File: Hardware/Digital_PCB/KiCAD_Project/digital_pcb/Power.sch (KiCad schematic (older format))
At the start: 24 parts, among them J6 Power, J7 Power Switch, U10 TPS793, U11 TPS1H000, U7 LT1521-3.3, U8 TEC 2-0921, U9 TPS723

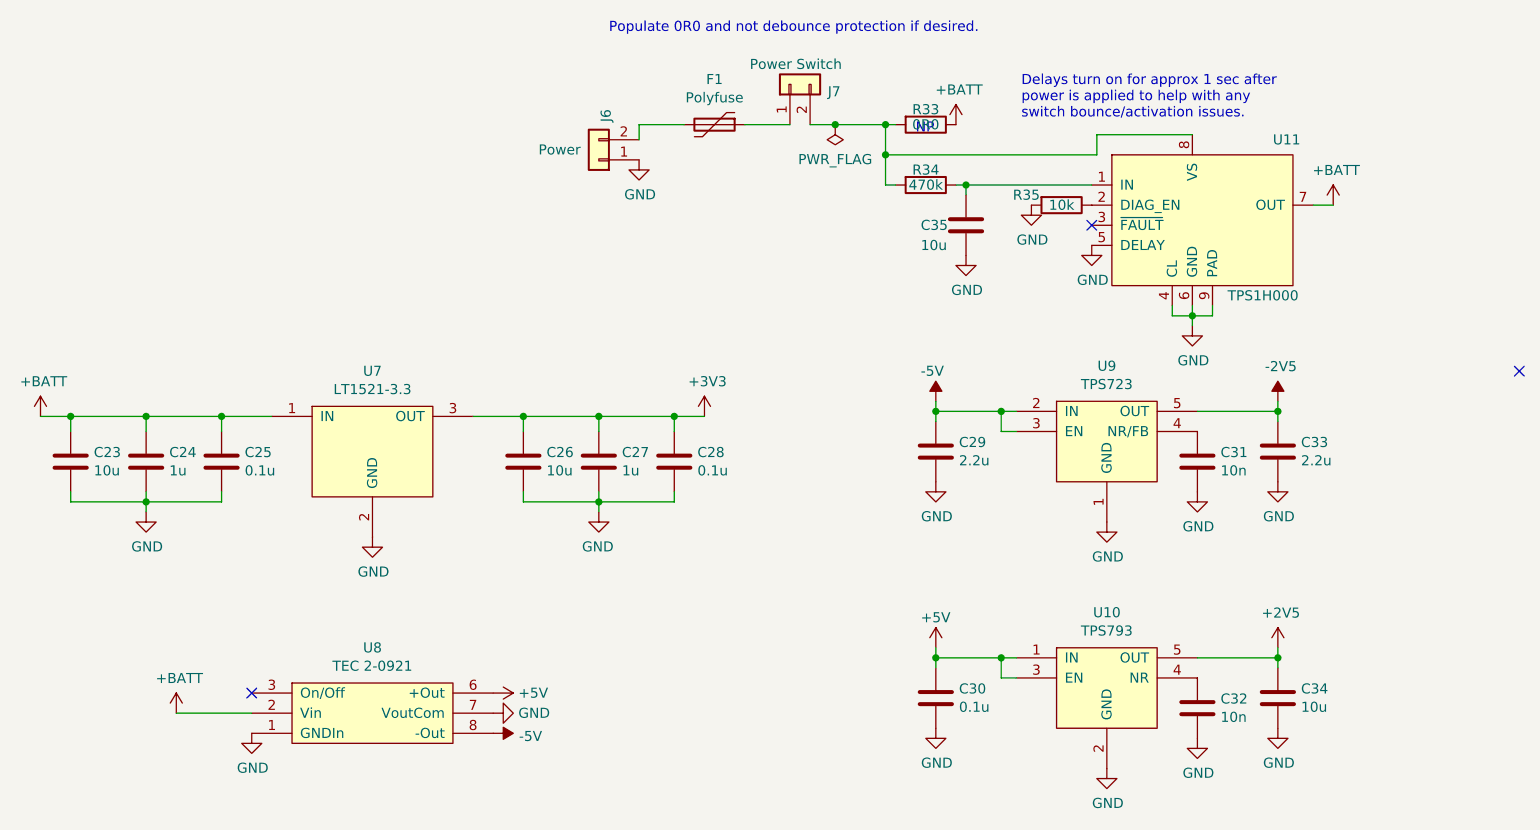
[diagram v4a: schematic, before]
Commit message: Update footprints
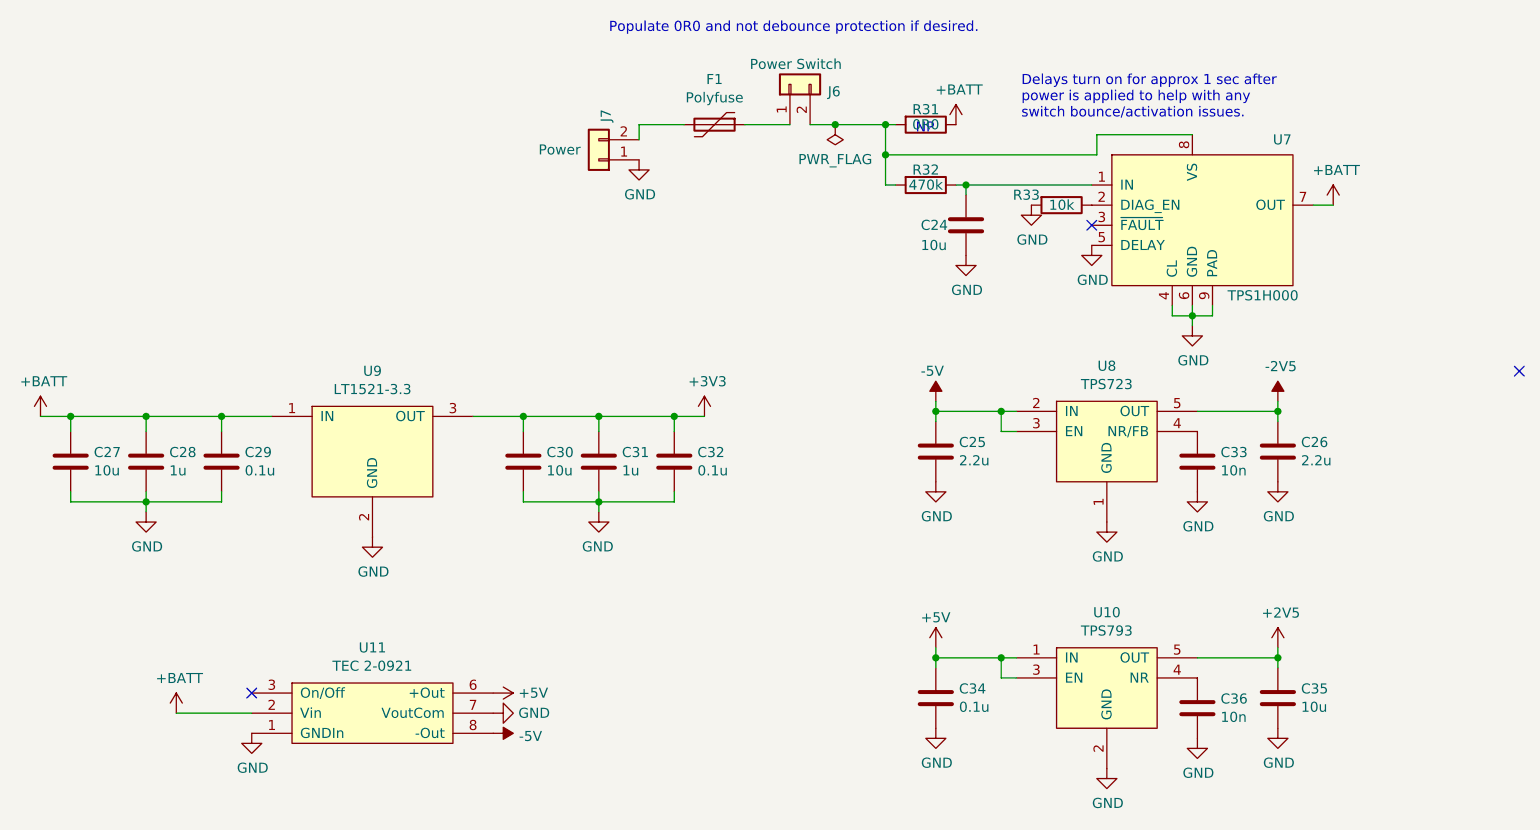
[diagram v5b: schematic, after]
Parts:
- C24: renamed from C35; footprint Capacitor_SMD:C_0805_2012Metric_Pad1.15x1.40mm_HandSolder -> Capacitor_SMD:C_0805_2012Metric
- C25: renamed from C29; footprint Capacitors_SMD:C_0603_HandSoldering -> Capacitor_SMD:C_0603_1608Metric
- C26: renamed from C33; footprint Capacitors_SMD:C_0603_HandSoldering -> Capacitor_SMD:C_0603_1608Metric
- C27: renamed from C23; footprint Capacitors_SMD:C_0805_HandSoldering -> Capacitor_SMD:C_0805_2012Metric
- C28: renamed from C24; footprint Capacitors_SMD:C_0603_HandSoldering -> Capacitor_SMD:C_0603_1608Metric
- C29: renamed from C25; footprint Capacitors_SMD:C_0603_HandSoldering -> Capacitor_SMD:C_0603_1608Metric
- C30: renamed from C26; footprint Capacitors_SMD:C_0805_HandSoldering -> Capacitor_SMD:C_0805_2012Metric
- C31: renamed from C27; footprint Capacitors_SMD:C_0603_HandSoldering -> Capacitor_SMD:C_0603_1608Metric
- C32: renamed from C28; footprint Capacitors_SMD:C_0603_HandSoldering -> Capacitor_SMD:C_0603_1608Metric
- C33: renamed from C31; footprint Capacitors_SMD:C_0603_HandSoldering -> Capacitor_SMD:C_0603_1608Metric
- C34: renamed from C30; footprint Capacitors_SMD:C_0603_HandSoldering -> Capacitor_SMD:C_0603_1608Metric
- C35: renamed from C34; footprint Capacitors_SMD:C_0805_HandSoldering -> Capacitor_SMD:C_0805_2012Metric
- C36: renamed from C32; footprint Capacitors_SMD:C_0603_HandSoldering -> Capacitor_SMD:C_0603_1608Metric
- J6: renamed from J7; footprint Pin_Headers:Pin_Header_Straight_1x02_Pitch2.54mm -> Connector_PinHeader_2.54mm:PinHeader_1x02_P2.54mm_Vertical
- J7: renamed from J6; footprint Pin_Headers:Pin_Header_Straight_1x02_Pitch2.54mm -> Connector_PinHeader_2.54mm:PinHeader_1x02_P2.54mm_Vertical
- R31: renamed from R33; footprint Resistor_SMD:R_0603_1608Metric_Pad1.05x0.95mm_HandSolder -> Resistor_SMD:R_0603_1608Metric
- R32: renamed from R34; footprint Resistor_SMD:R_0603_1608Metric_Pad1.05x0.95mm_HandSolder -> Resistor_SMD:R_0603_1608Metric
- R33: renamed from R35; footprint Resistor_SMD:R_0603_1608Metric_Pad1.05x0.95mm_HandSolder -> Resistor_SMD:R_0603_1608Metric
- U8: renamed from U9; footprint TO_SOT_Packages_SMD:SOT-23-5_HandSoldering -> Package_TO_SOT_SMD:SOT-23-5_HandSoldering
- renumbered U8 to U11, U11 to U7, U7 to U9
